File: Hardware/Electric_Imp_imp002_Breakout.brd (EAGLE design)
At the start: 160 x 100 mm, 2 parts

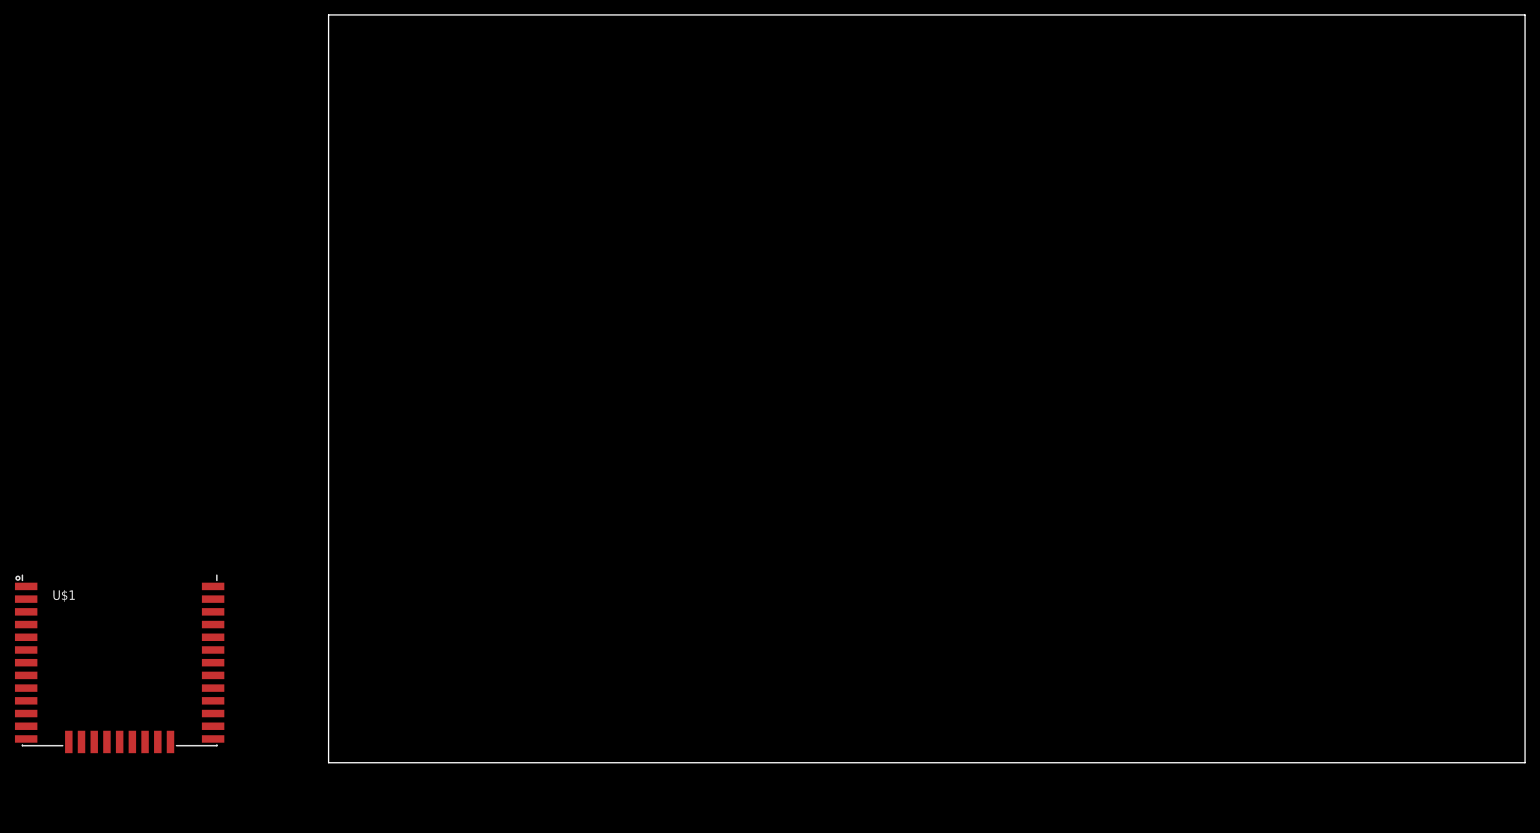
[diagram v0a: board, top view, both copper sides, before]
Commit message: Created initial schematic and part placement
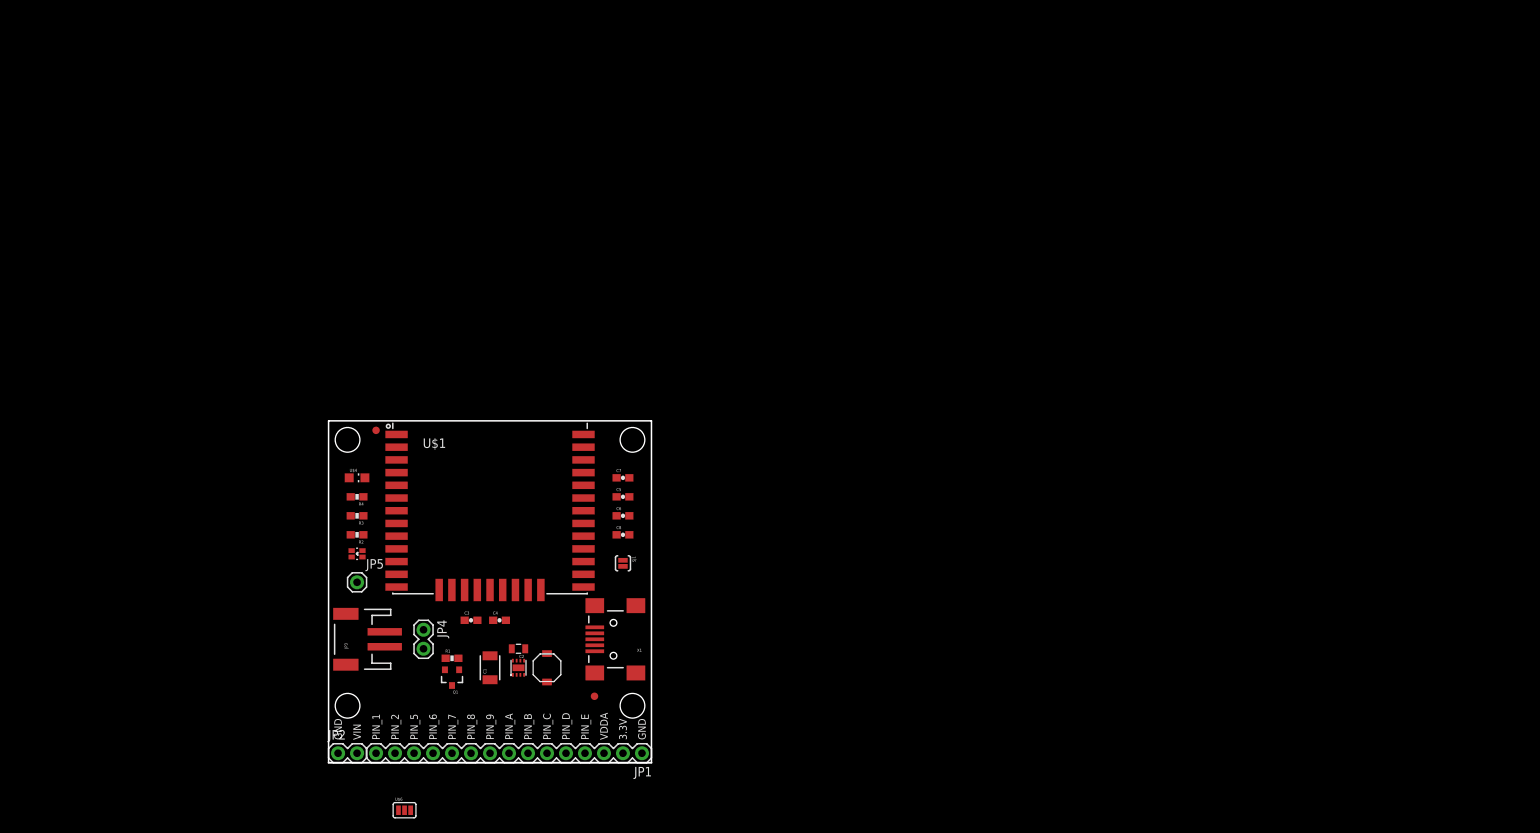
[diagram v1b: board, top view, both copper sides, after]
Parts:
- added C1: 10uF, SparkFun-Passives:1210
- added C2: 22uF, SparkFun-Passives:0805
- added C3, C5: 100pF, SparkFun-Capacitors:0603-CAP
- added C4, C6: 1.0uF, SparkFun-Capacitors:0603-CAP
- added C7, C8: DNP, SparkFun-Capacitors:0603-CAP
- added FID1, FID2: FIDUCIAL1X2, SparkFun-Aesthetics:FIDUCIAL-1X2
- added JP1: M15, SparkFun-Connectors:1X15
- added JP2, JP4: M02PTH, SparkFun-Connectors:1X02
- added JP3: M02-JST-2MM-SMT, SparkFun-Connectors:JST-2-SMD
- added JP5: M01PTH, SparkFun-Connectors:1X01
- added L1: 2.2uH, SparkFun-Passives:VLF4012A
- added Q1: DMG2307L-7, SparkFun-DiscreteSemi:SOT23-3
- added R1: 100k, SparkFun-Resistors:0603-RES
- added R2, R3: 330, SparkFun-Resistors:0603-RES
- added R4: 68k, SparkFun-Resistors:0603-RES
- added SJ1: JUMPER-PAD-2-NC_BY_PASTE, SparkFun-Passives:PAD-JUMPER-2-NC_BY_PASTE_YES_SILK
- added STANDOFF1, STANDOFF2, STANDOFF3, STANDOFF4: STAND-OFF, SparkFun-Electromechanical:STAND-OFF
- added U$4: PT17-21C-L41-TR8, Testing:PT17-21C-L41-TR8
- added U$5: LED-RG, SparkFun-LED:LTST-C195KGJRKT
- added U$6: JUMPER-PAD-3-2OF3_NC_BY_PASTE, SparkFun-Passives:PAD-JUMPER-3-2OF3_NC_BY_PASTE_YES_SILK_FULL_BOX
- added U2: TPS62172, SparkFun-PowerIC:WSON-8-PAD
- added X1: USBSMD, SparkFun-Connectors:USB-MINIB
- moved FRAME1 81.1 mm to (-15.2, -16.5)
- moved U$1 53.5 mm to (21.6, 38.1)
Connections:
- new net 3.3V: C2.1, C3.1, C4.1, C5.1, C6.1, JP1.2, L1.P$2, SJ1.2, U$1.18, U$1.33, U$5.P$1, U$5.P$2, U2.6
- new net GND: C1.2, C2.2, C3.2, C4.2, C5.2, C6.2, C7.2, C8.2, JP1.1, JP2.1, JP3.2, JP4.1, R1.1, R4.1, U$1.1, U$1.13, U$1.17, U$1.23, U$1.24, U$1.25, U$1.26, U$1.27, U$1.28, U$1.29, U$1.30, U$1.31, U$1.32, U$1.35, U$1.7, U2.1, U2.4, U2.5, U2.PAD, X1.GND
- new net LED_G: R3.1, U$1.3
- new net LED_R: R2.1, U$1.4
- new net N$1: L1.P$1, U2.7
- new net N$2: Q1.1, R1.2
- new net N$3: JP5.1, U$1.5
- new net N$4: R2.2, U$5.P$4
- new net N$5: R3.2, U$5.P$3
- new net N$6: Q1.2
- new net OPTO_BIAS: U$1.2, U$4.C
- new net OPTO_IN: R4.2, U$1.6, U$4.E
- new net PIN_1: JP1.15, U$1.15
- new net PIN_2: JP1.14, U$1.16
- new net PIN_5: JP1.13, U$1.19
- new net PIN_6: JP1.12, U$1.20
- new net PIN_7: JP1.11, U$1.21
- new net PIN_8: JP1.10, U$1.22
- new net PIN_9: JP1.9, U$1.14
- new net PIN_A: JP1.8, U$1.8
- new net PIN_B: JP1.7, U$1.9
- new net PIN_C: JP1.6, U$1.10
- new net PIN_D: JP1.5, U$1.11
- new net PIN_E: JP1.4, U$1.12
- new net VBAT: JP3.1, JP4.2, Q1.3
- new net VDDA: C7.1, C8.1, JP1.3, SJ1.1, U$1.34
- new net VIN: C1.1, JP2.2, U2.2, U2.3
- new net VUSB: X1.VBUS
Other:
- board size 160 x 100 mm -> 43.2 x 45.7 mm
- board text added: "3.3V"
- board text added: "GND"
- board text added: "PIN_1"
- board text added: "PIN_2"
- board text added: "PIN_5"
- board text added: "PIN_6"
- board text added: "PIN_7"
- board text added: "PIN_8"
- board text added: "PIN_9"
- board text added: "PIN_A"
- board text added: "PIN_B"
- board text added: "PIN_C"
- board text added: "PIN_D"
- board text added: "PIN_E"
- board text added: "VDDA"
- board text added: "VIN"

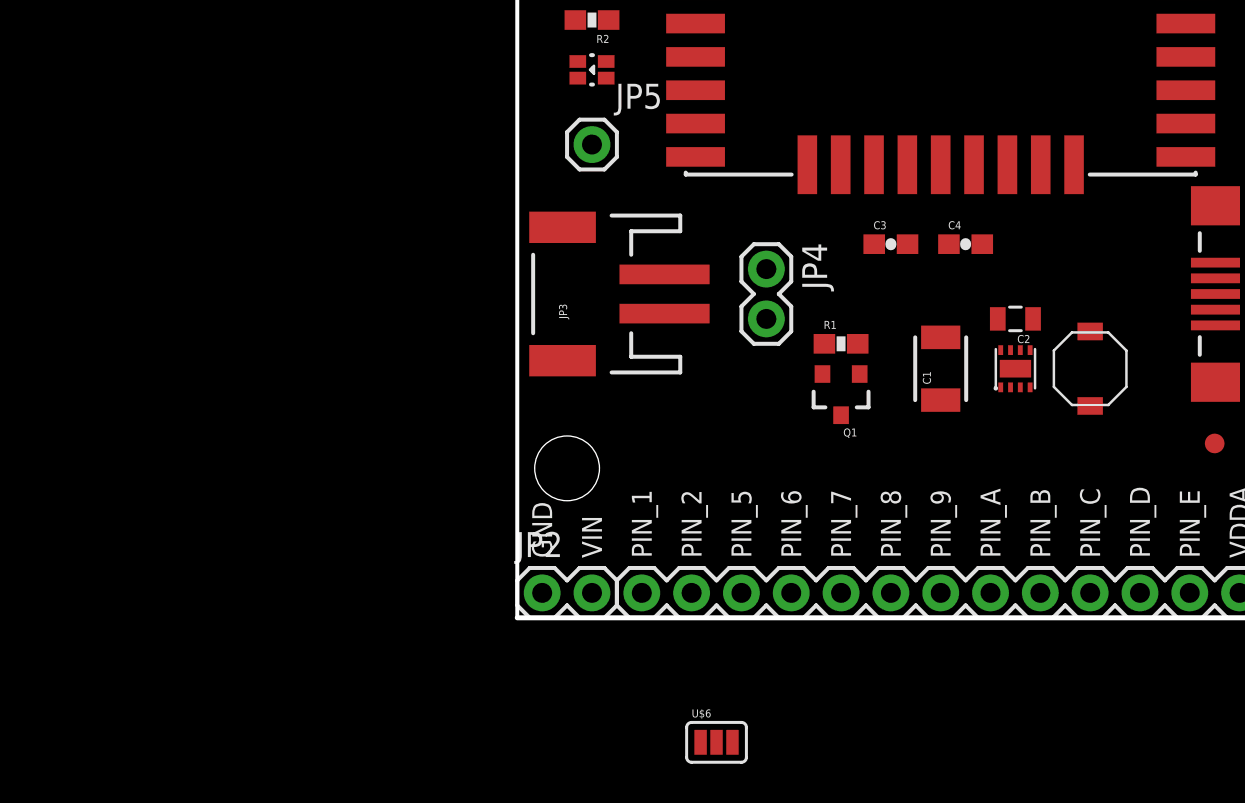
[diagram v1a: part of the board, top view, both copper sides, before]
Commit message: Added automatic voltage source selector and battery level monitor in schematic
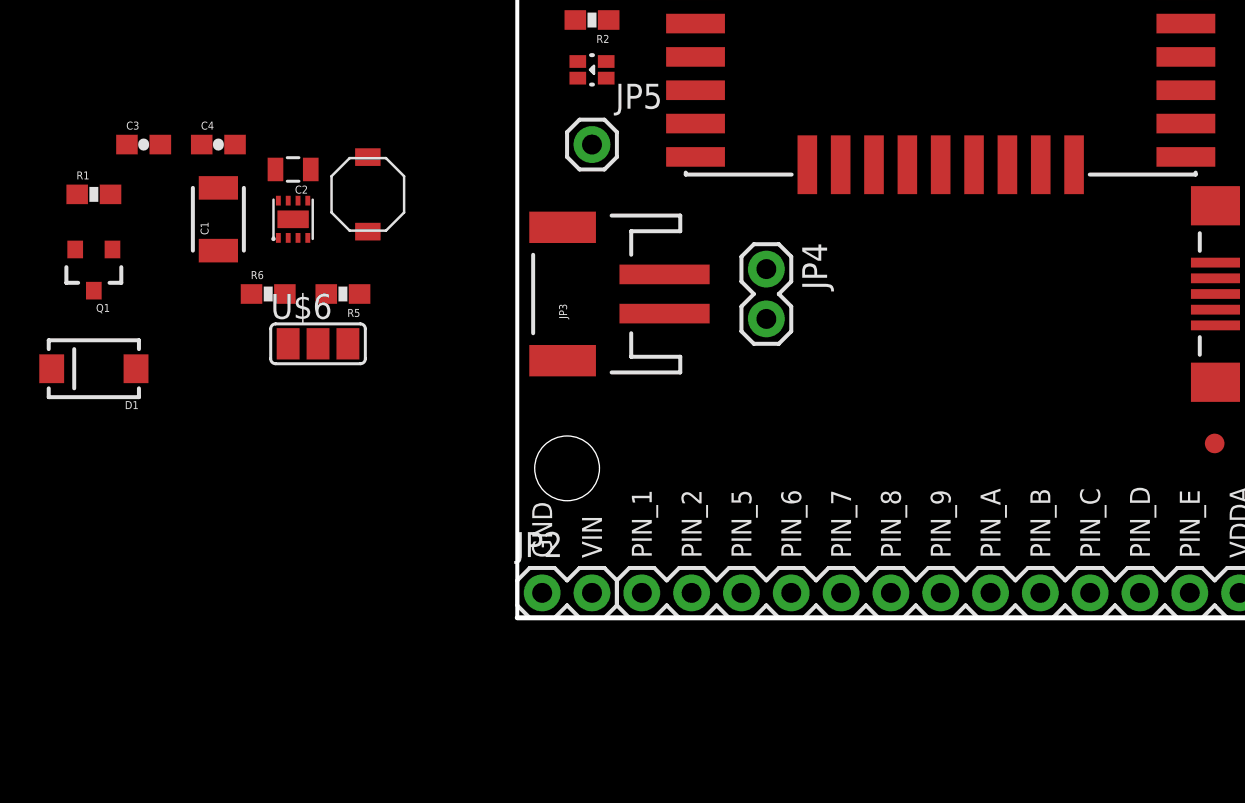
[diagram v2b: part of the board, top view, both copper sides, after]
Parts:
- added D1: MBRA140, SparkFun-DiscreteSemi:SMA-DIODE
- added R5, R6: 1M, SparkFun-Resistors:0603-RES
- U$5: value LED-RG -> LED-RGLTST-C195KGJRKT
- U$6: value JUMPER-PAD-3-2OF3_NC_BY_PASTE -> JUMPER-PAD-3-NOFULL_BOX_SILK; device SparkFun-Passives:PAD-JUMPER-3-2OF3_NC_BY_PASTE_YES_SILK_FULL_BOX -> SparkFun-Passives:PAD-JUMPER-3-NO_YES_SILK_FULL_BOX
- moved R1 38.9 mm to (-21.6, 21.6)
- moved Q1 38.6 mm to (-21.6, 17.8)
- moved C3 38.4 mm to (-19.1, 24.1)
- moved C4 38.4 mm to (-15.2, 24.1)
- moved L1 37.9 mm to (-7.62, 21.6)
- moved C1 37.6 mm to (-15.2, 20.3)
- moved C2 37.6 mm to (-11.4, 22.9)
- moved U2 37.6 mm to (-11.4, 20.3)
- moved U$6 28.7 mm to (-10.2, 14.0)
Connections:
- removed net VUSB: X1.VBUS
- new net N$7: R6.2, U$6.1
- net GND: now also R6.1
- net N$2: now also D1.A, X1.VBUS
- net N$6: now also R5.2, U$6.3; no longer Q1.2
- net PIN_A: now also U$6.2
- net VIN: now also D1.C, Q1.2, R5.1

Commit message: Finished v01 prototype for review
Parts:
- added LOGO1: OSHW-LOGOS, SparkFun-Aesthetics:OSHW-LOGO-S
- added LOGO2: SFE_LOGO_FLAME.1_INCH, SparkFun-Aesthetics:SFE_LOGO_FLAME_.1
- added TP1, TP2: TEST-POINT3X5, SparkFun-Passives:PAD.03X.05
- added U$9: SFE_LOGO_NAME_WEB, SparkFun-Aesthetics:SFE-NEW-WEBLOGO
- C7: value DNP -> 100pF
- moved D1 44.6 mm to (22.9, 9.53)
- moved Q1 40.7 mm to (19.1, 15.2), turned to 0 degrees
- moved C1 38.4 mm to (22.9, 15.2)
- moved C2 38.4 mm to (26.7, 17.8)
- moved U2 38.4 mm to (26.7, 15.2), turned to 270 degrees
- moved L1 38.3 mm to (30.5, 17.4)
- moved R1 38.0 mm to (15.9, 15.2), turned to 90 degrees
- moved C3 37.2 mm to (17.8, 19.1), turned to 180 degrees
- moved C4 37.2 mm to (21.6, 19.1)
- moved R5 26.5 mm to (16.5, 8.89)
- moved R6 25.3 mm to (11.4, 8.89)
- moved U$6 24.3 mm to (14.0, 11.4)
- moved SJ1 6.35 mm to (39.4, 33.0), turned to 180 degrees
- moved C6 5.08 mm to (39.4, 27.9)
- moved JP4 2.54 mm to (12.7, 15.2), turned to 90 degrees
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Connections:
- net N$3 renamed POWER_EN
- net GND: now also JP3.1; no longer JP3.2
- net OPTO_BIAS: now also TP1.P$1
- net OPTO_IN: now also TP2.P$1
- net PIN_1: now also JP1.10; no longer JP1.15
- net PIN_2: now also JP1.9; no longer JP1.14
- net PIN_5: now also JP1.8; no longer JP1.13
- net PIN_6: now also JP1.7; no longer JP1.12
- net PIN_7: now also JP1.6; no longer JP1.11
- net PIN_8: now also JP1.5; no longer JP1.10
- net PIN_9: now also JP1.4; no longer JP1.9
- net PIN_A: now also JP1.15; no longer JP1.8
- net PIN_B: now also JP1.14; no longer JP1.7
- net PIN_C: now also JP1.13; no longer JP1.6
- net PIN_D: now also JP1.12; no longer JP1.5
- net PIN_E: now also JP1.11; no longer JP1.4
- net VBAT: now also JP3.2; no longer JP3.1
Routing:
- net 3.3V: track 0.00 -> 97.7 mm, vias 0 -> 5
- net VDDA: track 0.00 -> 53.8 mm, vias 0 -> 1
- net PIN_A: track 0.00 -> 53.5 mm, vias 0 -> 3
- net PIN_9: track 0.00 -> 39.7 mm, vias 0 -> 2
- net VIN: track 0.00 -> 38.7 mm, vias 0 -> 2
- net PIN_B: track 0.00 -> 34.8 mm, vias 0 -> 1
- net PIN_C: track 0.00 -> 33.7 mm, vias 0 -> 1
- net PIN_D: track 0.00 -> 32.6 mm, vias 0 -> 1
- net PIN_5: track 0.00 -> 32.3 mm, vias 0 -> 1
- net PIN_E: track 0.00 -> 31.5 mm, vias 0 -> 1
- net PIN_6: track 0.00 -> 31.0 mm, vias 0 -> 1
- net PIN_7: track 0.00 -> 29.7 mm, vias 0 -> 1
- net PIN_8: track 0.00 -> 28.4 mm, vias 0 -> 1
- net PIN_2: track 0.00 -> 28.4 mm, vias 0 -> 1
- net PIN_1: track 0.00 -> 28.0 mm, vias 0 -> 1
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- added copper zone on layer 1, net GND
- added copper zone on layer 16, net GND
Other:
- board text added: "OPTO_BIAS"
- board text added: "OPTO_IN"
- board text added: "PWR_EN"
- board text added: "Shawn Hymel (SparkFun Electronics) Based on Electric Imp's Amber board"
- board text added: "VDD"
- board text added: "imp002 Breakout"
- board text added: "v01"

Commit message: Made changes from review. Fixed VIn sense divider. Updated packages to remove $ symbols. Added +/- silk to battery. Added voltage input range text on sch and brd. Moved decoup caps on bottom of imp to remove loop.
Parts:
- removed U$4: PT17-21C-L41-TR8, Testing:PT17-21C-L41-TR8
- added Q2: PHOTOTRANSISTORPT17-21C-L41-TR8, SparkFun-DiscreteSemi:PT17-21C-L41-TR8
- R5: value 1M -> 33k
- R6: value 1M -> 62k
- moved C3 3.86 mm to (21.6, 19.7), turned to 270 degrees
- moved C4 2.62 mm to (24.1, 19.7), turned to 270 degrees
- renumbered U$1 to U1, U$5 to D2
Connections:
- net OPTO_BIAS: now also Q2.C; no longer U$4.C
- net OPTO_IN: now also Q2.E; no longer U$4.E
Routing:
- net 3.3V: track 97.7 -> 93.5 mm
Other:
- board text added: "+"
- board text added: "-"
- board text added: "VIN = 3.3 - 17V"

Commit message: Changed 68k resistor to 62k
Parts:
- R4: value 68k -> 62k
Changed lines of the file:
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@@
 <setting verticaltext="up"/>
 </settings>
-<grid distance="0.01" unitdist="inch" unit="inch" style="dots" multiple="1" display="yes" altdistance="0.005" altunitdist="inch" altunit="inch"/>
+<grid distance="0.05" unitdist="inch" unit="inch" style="dots" multiple="1" display="yes" altdistance="0.005" altunitdist="inch" altunit="inch"/>
 <layers>
 <layer number="1" name="Top" color="4" fill="1" visible="yes" active="yes"/>
@@
 <attribute name="PROD_ID" value="RES-00818" x="3.81" y="33.02" size="1.778" layer="27" font="vector" ratio="15" rot="R180" display="off"/>
 </element>
-<element name="R4" library="SparkFun-Resistors" package="0603-RES" value="68k" x="3.81" y="35.56" rot="R180"/>
+<element name="R4" library="SparkFun-Resistors" package="0603-RES" value="62k" x="3.81" y="35.56" rot="R180"/>
 <element name="JP1" library="SparkFun-Connectors" package="1X15" value="M15" x="41.91" y="1.27" rot="R180"/>
 <element name="JP5" library="SparkFun-Connectors" package="1X01" value="M01PTH" x="3.81" y="22.86"/>
